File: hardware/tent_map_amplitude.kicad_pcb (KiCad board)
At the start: 4 copper layers, 56.4 x 60.2 mm, 50 parts, among them U1 LM339AN, U2 TL082IP, U3 TL082IP, U4 LF398_DIP8, U5 LF398_DIP8, U6 LF398_DIP8

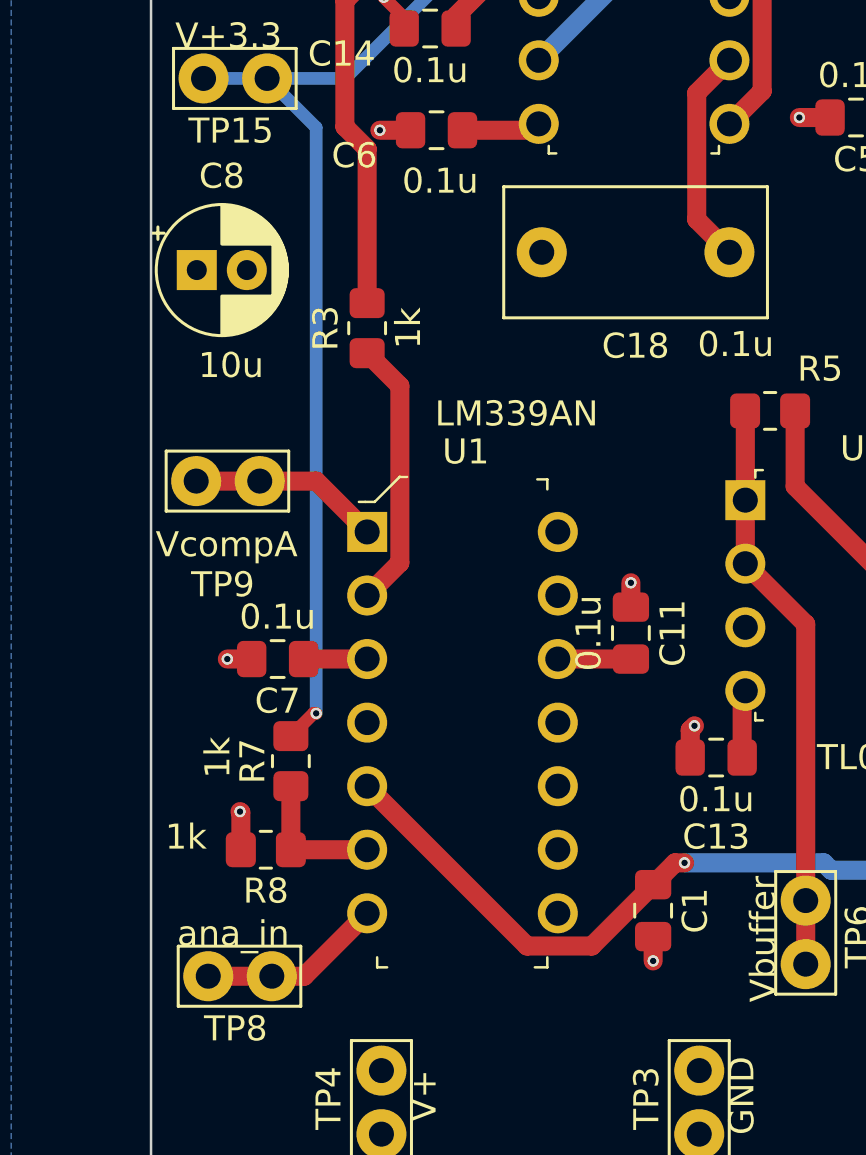
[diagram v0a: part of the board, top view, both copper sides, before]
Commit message: Move big cap, route trace through legs of dip package
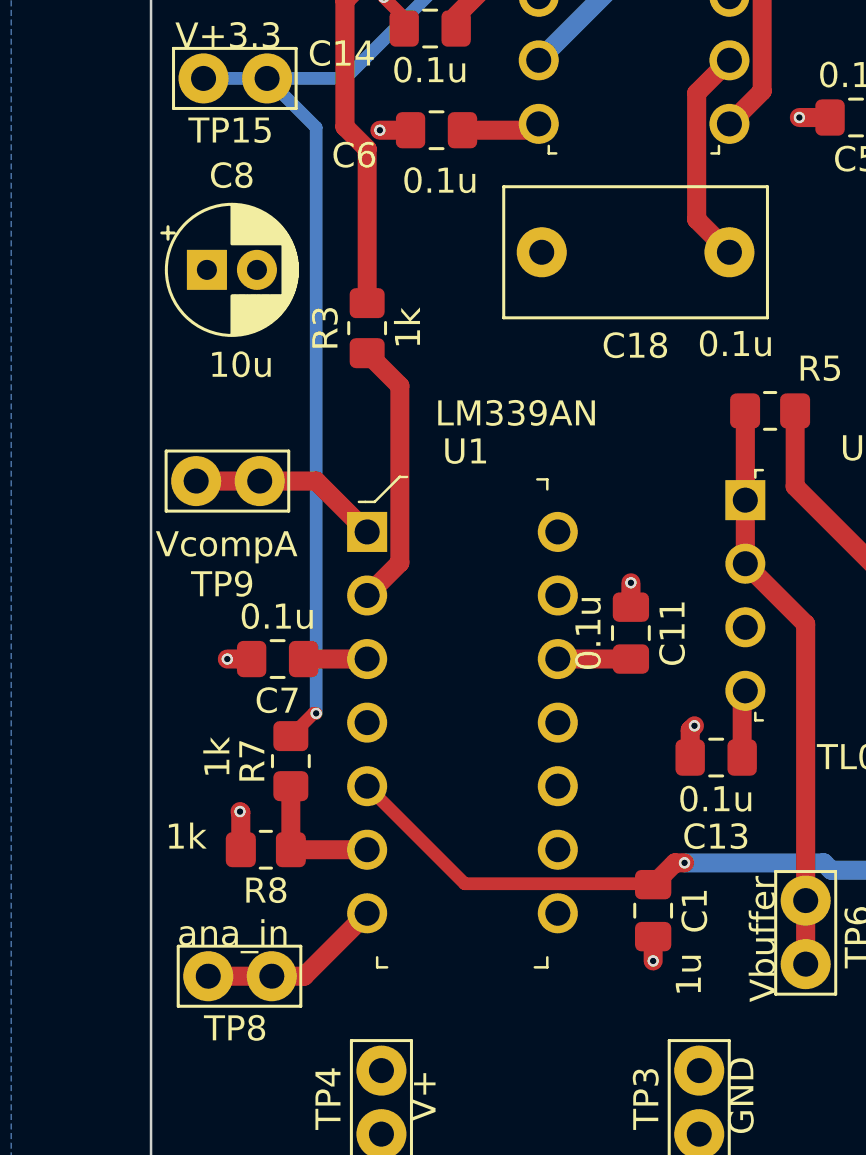
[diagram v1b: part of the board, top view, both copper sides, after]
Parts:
- moved C8 0.40 mm to (68.8, 77.2)
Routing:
- net Net-(C1-Pad1): track 86.7 -> 84.6 mm
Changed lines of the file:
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@@
   )
   (setup
-    (last_trace_width 0.762)
+    (last_trace_width 0.508)
     (user_trace_width 0.127)
     (user_trace_width 0.254)
@@
   )
   (module Capacitor_THT:CP_Radial_D5.0mm_P2.00mm (layer Front)
-    (at 68.3768 77.216)
+    (at 68.78066 77.20838)
     (descr "CP, Radial series, Radial, pin pitch=2.00mm, , diameter=5mm, Electrolytic Capacitor")
     (tags "CP Radial series Radial pin pitch 2.00mm  diameter 5mm Electrolytic Capacitor")
@@
       (effects (font (size 1 1) (thickness 0.15)))
     )
-    (fp_text value 1u (at 0 1.68 90) (layer F.Fab)
+    (fp_text value 1u (at 2.55152 -1.44272 90) (layer F.SilkS)
       (effects (font (size 1 1) (thickness 0.15)))
     )
@@
   (segment (start 100.965 94.5388) (end 98.425 94.5388) (width 0.762) (layer Front) (net 2))
   (segment (start 111.6584 57.9628) (end 111.6584 55.4228) (width 0.762) (layer Back) (net 2))
-  (segment (start 81.572001 104.228801) (end 75.184 97.8408) (width 0.762) (layer Front) (net 2))
-  (segment (start 84.162999 104.228801) (end 81.572001 104.228801) (width 0.762) (layer Front) (net 2))
-  (segment (start 86.614 101.7778) (end 84.162999 104.228801) (width 0.762) (layer Front) (net 2))
   (segment (start 99.806579 95.920379) (end 97.917 94.0308) (width 0.762) (layer Back) (net 2))
   (segment (start 99.806579 98.714379) (end 99.806579 95.920379) (width 0.762) (layer Back) (net 2))
@@
   (segment (start 114.414201 69.913401) (end 114.414201 75.857199) (width 0.762) (layer Back) (net 2))
   (segment (start 113.1062 68.6054) (end 114.414201 69.913401) (width 0.762) (layer Back) (net 2))
+  (segment (start 79.082999 101.739799) (end 75.184 97.8408) (width 0.508) (layer Front) (net 2))
+  (segment (start 86.575999 101.739799) (end 79.082999 101.739799) (width 0.508) (layer Front) (net 2))
+  (segment (start 86.614 101.7778) (end 86.575999 101.739799) (width 0.508) (layer Front) (net 2))
   (segment (start 95.758 71.12) (end 98.298 71.12) (width 0.762) (layer Front) (net 3))
   (segment (start 81.788 71.628) (end 82.042 71.374) (width 0.762) (layer Front) (net 3))

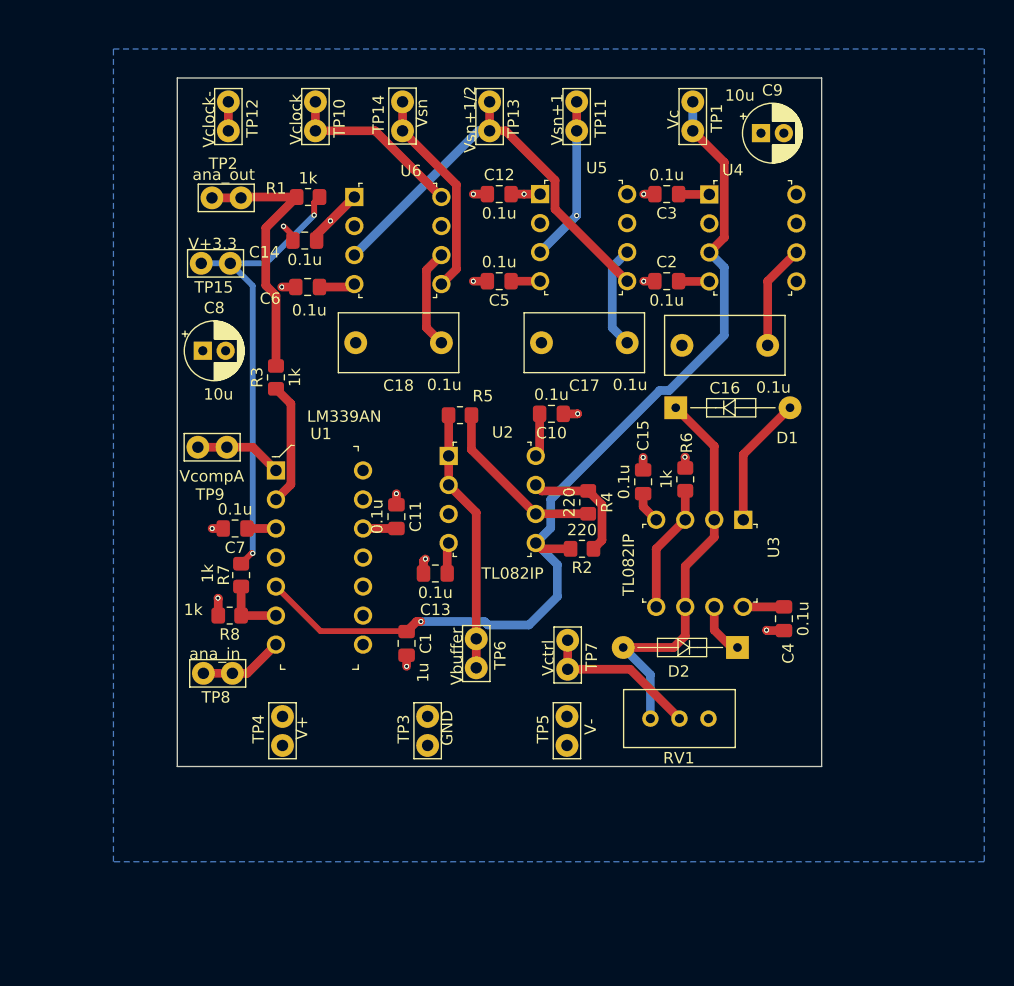
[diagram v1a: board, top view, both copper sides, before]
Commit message: Add extra cap footprints, change trace tolerance to 10thou, Add second variable resistor
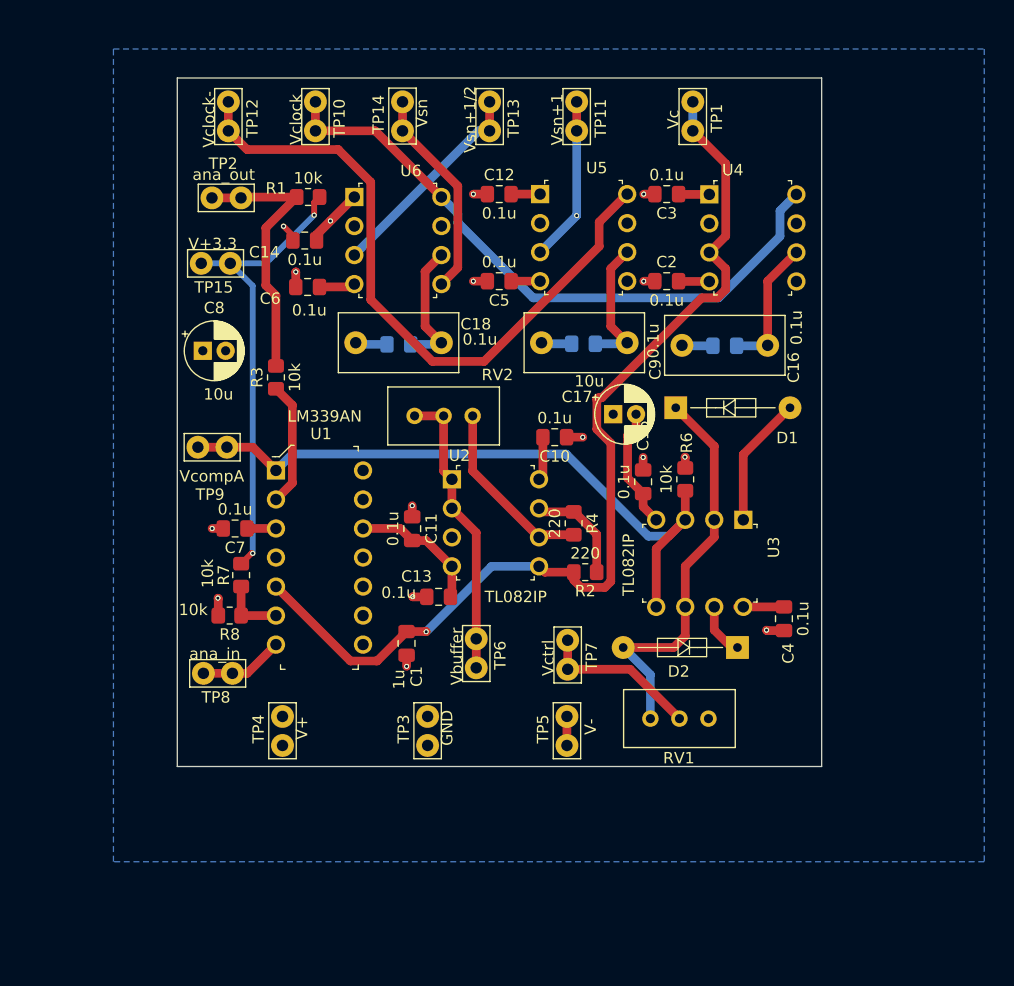
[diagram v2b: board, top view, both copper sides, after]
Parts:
- removed R5: 2k, Resistor_SMD:R_0805_2012Metric_Pad1.20x1.40mm_HandSolder
- added CE1: dnp, Capacitor_SMD:C_0805_2012Metric_Pad1.18x1.45mm_HandSolder, B.Cu at (114.5, 76.8)
- added CE2: dnp, Capacitor_SMD:C_0805_2012Metric_Pad1.18x1.45mm_HandSolder, B.Cu at (102.1, 76.6)
- added CE3: dnp, Capacitor_SMD:C_0805_2012Metric_Pad1.18x1.45mm_HandSolder, B.Cu at (85.9, 76.7)
- added RV2: R_POT, Potentiometer_THT:Potentiometer_Bourns_3296W_Vertical, F.Cu at (92.4, 82.9)
- R1, R3, R6, R7, R8: value 1k -> 10k
- moved C9 27.8 mm to (104.7, 82.8)
- moved R4 2.23 mm to (101.2, 92.3)
- moved C13 2.06 mm to (89.4, 98.7)
- moved R2 2.06 mm to (102.2, 96.6)
- moved U2 2.06 mm to (90.6, 88.5)
- moved C10 2.06 mm to (99.6, 84.8)
- moved C11 1.74 mm to (87.1, 92.8)
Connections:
- U1 pad 10: (no net) -> GND
- U1 pad 11: (no net) -> V+
- U1 pad 13: (no net) -> Net-(U1-Pad13)
- U1 pad 14: (no net) -> Net-(U1-Pad14)
- U1 pad 8: (no net) -> GND
- U1 pad 9: (no net) -> V+
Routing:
- net V-: track 16.8 -> 114.5 mm
- net Net-(TP12-Pad1): track 39.7 -> 59.1 mm
- net GND: track 17.0 -> 25.3 mm
- net Net-(TP10-Pad1): track 48.9 -> 56.2 mm
- net Net-(TP11-Pad1): track 36.1 -> 39.3 mm
- net Net-(R6-Pad2): track 61.9 -> 58.9 mm
- net Net-(C17-Pad1): track 9.01 -> 11.9 mm
- net Net-(C18-Pad1): track 8.75 -> 11.6 mm
- net Net-(C16-Pad1): track 9.17 -> 11.9 mm
- net Net-(C1-Pad1): track 84.6 -> 87.3 mm
- net Net-(RV2-Pad2): track 23.1 -> 25.8 mm
- net Net-(RV1-Pad2): track 29.5 -> 28.0 mm
- net Net-(R2-Pad1): track 10.7 -> 9.30 mm
- net Net-(R4-Pad2): track 15.6 -> 16.2 mm
- net V+: vias 3 -> 2
- added copper zone on B.Cu, net GND
- removed copper zone on B.Cu, net V-
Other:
- net class Default: clearance 0.127 -> 0.254; trace_width 0.127 -> 0.254
- rule trace_clearance: 0.127 -> 0.254
- rule trace_min: 0.127 -> 0.254

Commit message: Add 3.5mm mounting holes
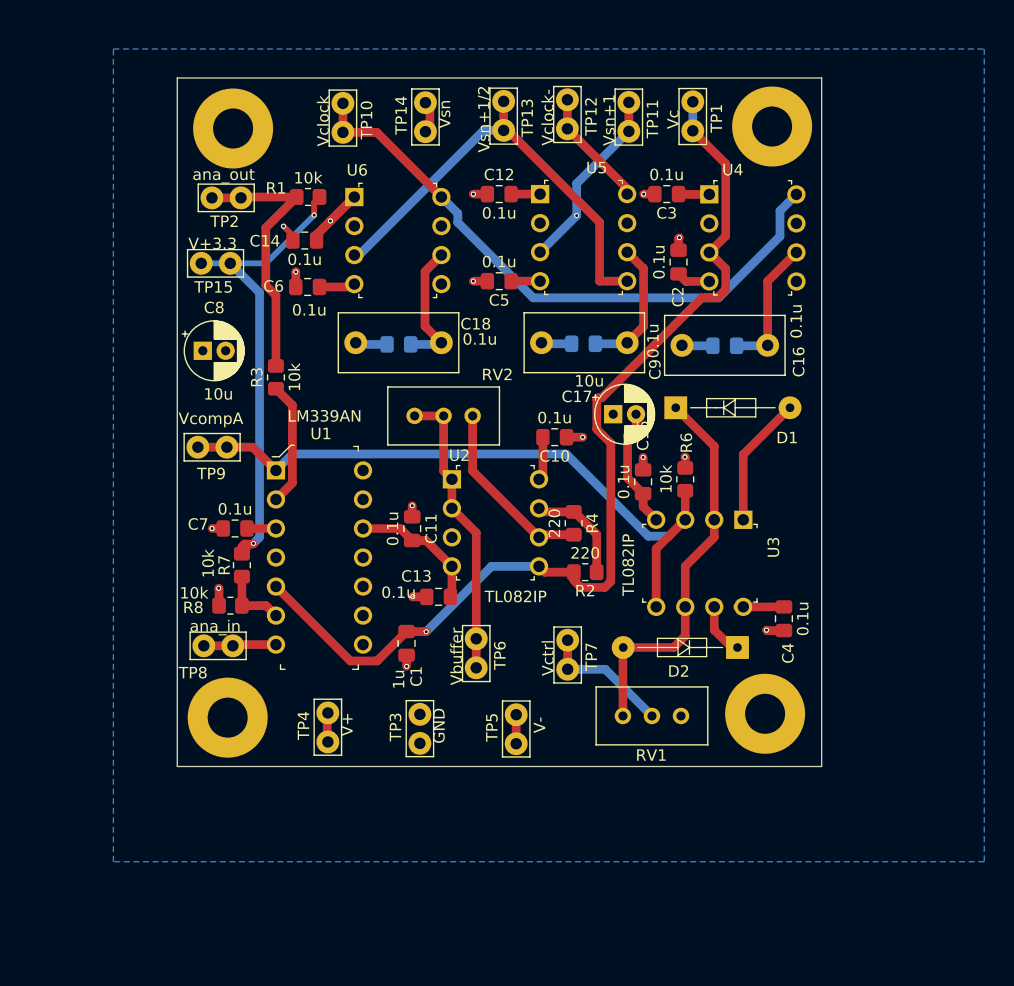
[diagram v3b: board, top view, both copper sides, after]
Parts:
- added Mnt1: MountingHole_3.5mm_Pad, MountingHole:MountingHole_3.5mm_Pad, F.Cu at (118.6, 57.6)
- added REF**: MountingHole_3.5mm_Pad, MountingHole:MountingHole_3.5mm_Pad, F.Cu at (71.0, 109.3)
- added REF**: MountingHole_3.5mm_Pad, MountingHole:MountingHole_3.5mm_Pad, F.Cu at (118.0, 109.0)
- added REF**: MountingHole_3.5mm_Pad, MountingHole:MountingHole_3.5mm_Pad, F.Cu at (71.4, 57.8)
- moved TP12 29.7 mm to (100.7, 57.8)
- moved TP11 4.56 mm to (106.1, 58.0)
- moved TP5 4.44 mm to (96.2, 109.1)
- moved TP4 3.98 mm to (79.7, 108.9)
- moved RV1 2.41 mm to (105.5, 109.2)
- moved TP10 2.41 mm to (81.0, 58.1)
- moved TP8 2.41 mm to (68.9, 103.0)
- moved TP14 2.01 mm to (88.3, 55.5)
- moved C2 1.97 mm to (110.4, 69.4), turned to 270 degrees
- moved TP13 1.23 mm to (95.1, 57.9)
- moved R7 0.87 mm to (72.2, 96.0)
- moved R8 0.87 mm to (71.2, 99.5)
- moved TP3 0.70 mm to (87.8, 109.0)
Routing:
- net Net-(TP12-Pad1): track 59.1 -> 10.4 mm
- net V+: track 26.5 -> 29.0 mm
- net Net-(RV1-Pad2): track 28.0 -> 25.5 mm
- net Net-(TP10-Pad1): track 56.2 -> 53.7 mm
- net Net-(TP14-Pad1): track 18.5 -> 16.5 mm
- net Net-(TP11-Pad1): track 39.3 -> 41.1 mm
- net Net-(TP13-Pad1): track 38.0 -> 39.4 mm
- net V-: track 114.5 -> 113.2 mm
- net +3V3: track 41.0 -> 42.3 mm
- net Net-(D1-Pad1): track 35.5 -> 34.3 mm
- net Net-(TP8-Pad1): track 7.39 -> 6.36 mm

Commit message: Move traces off of ground and power planes
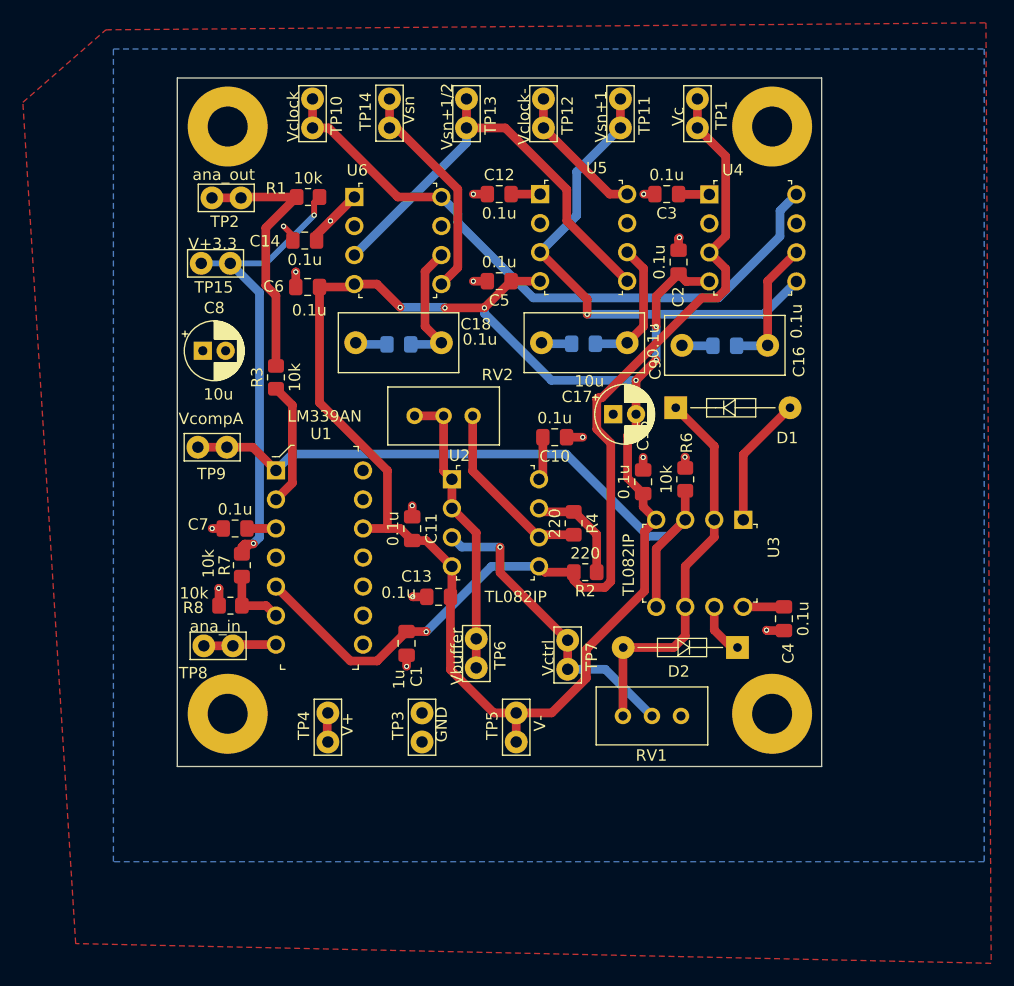
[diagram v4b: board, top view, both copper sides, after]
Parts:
- moved TP13 3.26 mm to (91.9, 57.7)
- moved TP14 3.16 mm to (85.1, 55.2)
- moved TP10 2.69 mm to (78.4, 57.7)
- moved TP12 2.10 mm to (98.6, 57.7)
- moved TP11 0.79 mm to (105.3, 57.7)
- moved REF** 0.61 mm to (118.6, 109.0)
- moved REF** 0.50 mm to (71.0, 57.6)
- moved TP1 0.48 mm to (112.1, 57.7)
- moved REF** 0.34 mm to (71.0, 109.0)
- moved TP3 0.22 mm to (88.0, 108.9)
- moved TP5 0.15 mm to (96.2, 108.9)
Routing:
- net V-: track 113.2 -> 140.3 mm, vias 0 -> 6
- net Net-(TP14-Pad1): track 16.5 -> 19.6 mm
- net Net-(TP10-Pad1): track 53.7 -> 56.6 mm
- net Net-(TP12-Pad1): track 10.4 -> 12.3 mm
- net Net-(TP11-Pad1): track 41.1 -> 43.0 mm
- net Net-(RV1-Pad2): track 25.5 -> 26.8 mm, vias 0 -> 1
- added copper zone on F.Cu, net GND
